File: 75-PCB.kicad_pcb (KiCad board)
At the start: 2 copper layers, 324 parts, among them J1 AVR-ISP-6, Q1 2N7002, SW1 SW_Push, U1 AT90USB1286-AU, U2 PRTR5V0U2X, Y1 16MHz

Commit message: Finished PCB edges
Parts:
- moved USB1 257.2 mm to (283.4, -240.5), turned to 180 degrees
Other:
- board outline added: 315.1 x 125.4 mm

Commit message: Changed USB connector
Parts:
- LED1, LED2, LED3, LED4, LED5, LED6, LED7, LED8, LED9, U1, U2: moved to B.Cu
- USB1: value Wurth-632723300011 -> HRO-TYPE-C-31-M-12; footprint Type-C:Wurth-632723300011-HandSoldering -> Type-C:HRO-TYPE-C-31-M-12
- moved SW1 524.7 mm to (324.6, -208.0)
- moved D1 520.4 mm to (358.8, -217.5)
- moved LED5 507.3 mm to (258.8, -231.0), turned to 270 degrees
- moved J1 498.0 mm to (283.4, -198.4)
- moved LED8 494.6 mm to (304.0, -196.1)
- moved LED4 470.0 mm to (199.2, -231.0), turned to 90 degrees
- moved LED9 454.7 mm to (304.0, -158.0)
- moved R9 454.5 mm to (392.8, -184.2)
- moved R8 445.0 mm to (384.0, -184.2)
- moved LED3 438.4 mm to (133.3, -231.0), turned to 270 degrees
- moved F1 431.8 mm to (349.1, -169.9)
- moved LED1 431.7 mm to (11.9, -231.0), turned to 90 degrees
- moved LED2 429.7 mm to (73.0, -231.0), turned to 270 degrees
- moved U2 428.9 mm to (289.7, -227.8)
- moved C11 393.7 mm to (348.3, -152.4)
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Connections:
- U1 pad 17: Net-(U1-Pad17) -> LEDMOS
- USB1 pad 10: Net-(USB1-Pad10) -> Net-(R7-Pad2)
- USB1 pad 11: Net-(USB1-Pad11) -> VCC
- USB1 pad 2: Net-(USB1-Pad2) -> VCC
- USB1 pad 4: VCC -> Net-(R6-Pad2)
- USB1 pad 5: Net-(R6-Pad2) -> Net-(R8-Pad2)
- USB1 pad 8: Net-(USB1-Pad8) -> Net-(R9-Pad2)
- USB1 pad 9: VCC -> Net-(USB1-Pad9)
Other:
- net class Default: trace_width 0.25 -> 0.254
- net class Power added: clearance 0.2, trace_width 0.381, via_dia 0.8, via_drill 0.4

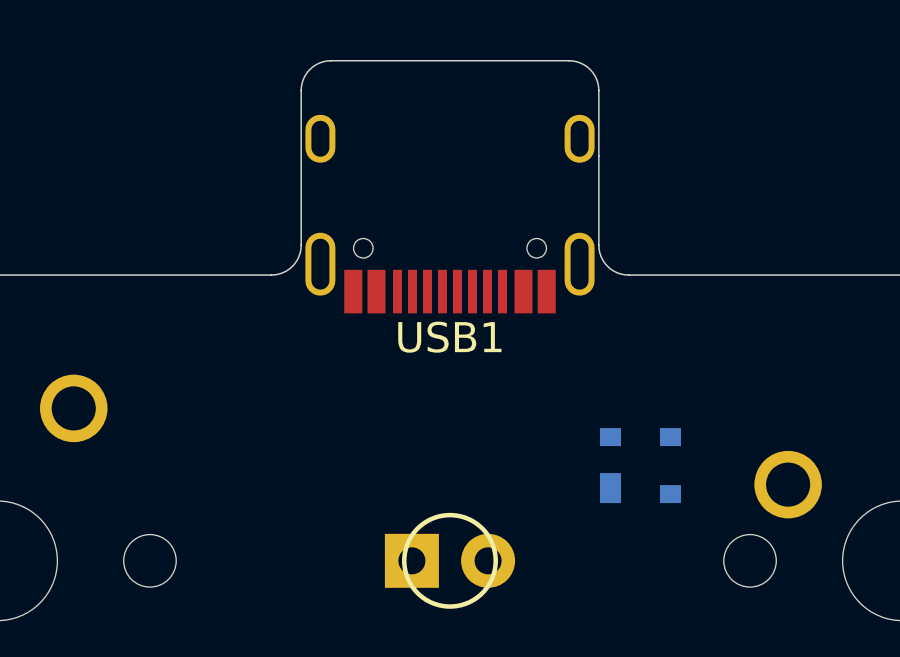
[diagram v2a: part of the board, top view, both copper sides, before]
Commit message: Changed USB connector
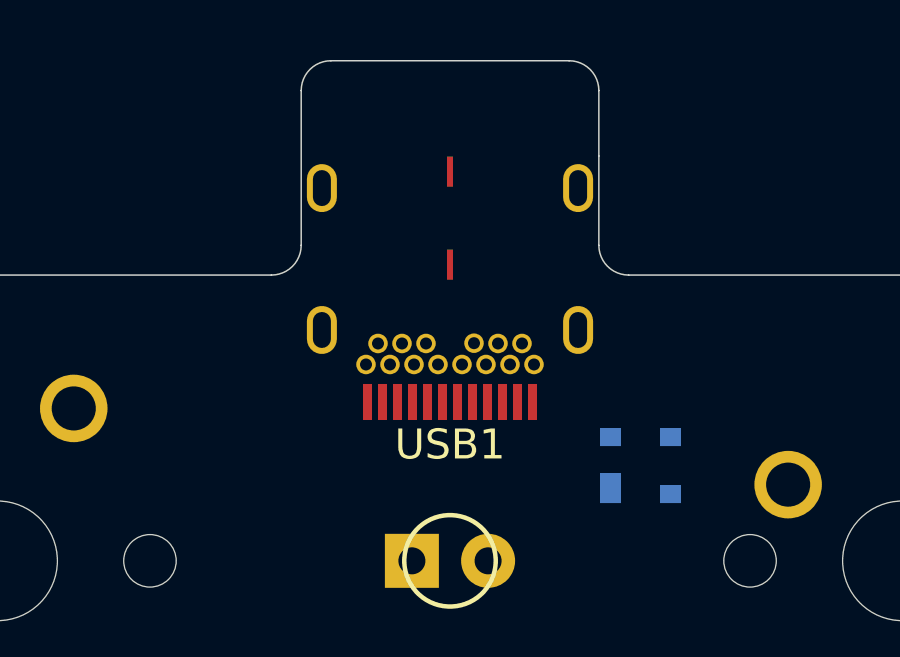
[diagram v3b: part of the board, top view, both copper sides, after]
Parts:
- USB1: value HRO-TYPE-C-31-M-12 -> Wurth-632723300011; footprint Type-C:HRO-TYPE-C-31-M-12 -> Type-C:Wurth-632723300011
- moved USB1 0.79 mm to (283.4, -240.5)
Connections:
- USB1 pad 10: Net-(R7-Pad2) -> Net-(USB1-Pad10)
- USB1 pad 11: VCC -> Net-(USB1-Pad11)
- USB1 pad 2: VCC -> Net-(USB1-Pad2)
- USB1 pad 4: Net-(R6-Pad2) -> VCC
- USB1 pad 5: Net-(R8-Pad2) -> Net-(R6-Pad2)
- USB1 pad 8: Net-(R9-Pad2) -> Net-(USB1-Pad8)
- USB1 pad 9: Net-(USB1-Pad9) -> VCC
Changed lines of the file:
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@@
     (zones 0)
     (modules 324)
-    (nets 285)
+    (nets 293)
   )
   (page A4)
@@
   (net 282 "Net-(USB1-Pad3)")
   (net 283 "Net-(MX_#0-Pad4)")
-  (net 284 "Net-(USB1-Pad9)")
+  (net 284 "Net-(USB1-Pad23)")
+  (net 285 "Net-(USB1-Pad22)")
+  (net 286 "Net-(USB1-Pad20)")
+  (net 287 "Net-(USB1-Pad15)")
+  (net 288 "Net-(USB1-Pad14)")
+  (net 289 "Net-(USB1-Pad11)")
+  (net 290 "Net-(USB1-Pad10)")
+  (net 291 "Net-(USB1-Pad8)")
+  (net 292 "Net-(USB1-Pad2)")
   (net_class Default "This is the default net class."
     (clearance 0.2)
@@
     (add_net "Net-(U1-Pad62)")
     (add_net "Net-(U1-Pad9)")
+    (add_net "Net-(USB1-Pad10)")
+    (add_net "Net-(USB1-Pad11)")
+    (add_net "Net-(USB1-Pad14)")
+    (add_net "Net-(USB1-Pad15)")
+    (add_net "Net-(USB1-Pad2)")
+    (add_net "Net-(USB1-Pad20)")
+    (add_net "Net-(USB1-Pad22)")
+    (add_net "Net-(USB1-Pad23)")
     (add_net "Net-(USB1-Pad3)")
-    (add_net "Net-(USB1-Pad9)")
+    (add_net "Net-(USB1-Pad8)")
     (add_net RESET)
     (add_net RGBLED)
@@
     (add_net VCC)
   )
-  (module Type-C:HRO-TYPE-C-31-M-12 (layer F.Cu)
-    (at 283.36875 -241.3 180)
+  (module Type-C:Wurth-632723300011 (layer F.Cu)
+    (at 283.36875 -240.50625 180)
     (attr smd)
-    (fp_text reference USB1 (at 0 -9.25) (layer F.SilkS)
+    (fp_text reference USB1 (at 0 -12) (layer F.SilkS)
       (effects (font (size 1 1) (thickness 0.15)))
     )
-    (fp_text value HRO-TYPE-C-31-M-12 (at 0 1.15) (layer Dwgs.User)
+    (fp_text value Wurth-632723300011 (at 0 1.9) (layer F.Fab)
       (effects (font (size 1 1) (thickness 0.15)))
     )
-    (fp_line (start -4.47 0) (end 4.47 0) (layer Dwgs.User) (width 0.15))
-    (fp_line (start -4.47 0) (end -4.47 -7.3) (layer Dwgs.User) (width 0.15))
-    (fp_line (start 4.47 0) (end 4.47 -7.3) (layer Dwgs.User) (width 0.15))
-    (fp_line (start -4.47 -7.3) (end 4.47 -7.3) (layer Dwgs.User) (width 0.15))
-    (pad 12 smd rect (at 3.225 -7.695 180) (size 0.6 1.45) (layers F.Cu F.Paste F.Mask)
-      (net 1 GND))
-    (pad 1 smd rect (at -3.225 -7.695 180) (size 0.6 1.45) (layers F.Cu F.Paste F.Mask)
-      (net 1 GND))
-    (pad 11 smd rect (at 2.45 -7.695 180) (size 0.6 1.45) (layers F.Cu F.Paste F.Mask)
+    (fp_line (start -4.37 0.95) (end 4.37 0.95) (layer Dwgs.User) (width 0.15))
+    (fp_line (start -4.37 0.95) (end -4.37 -10.38) (layer Dwgs.User) (width 0.15))
+    (fp_line (start 4.37 0.95) (end 4.37 -10.38) (layer Dwgs.User) (width 0.15))
+    (fp_line (start -4.37 -10.38) (end 4.37 -10.38) (layer Dwgs.User) (width 0.15))
+    (pad 27 smd rect (at 0 -2.9 180) (size 0.2 1) (layers F.Cu F.Paste F.Mask)
+      (net 1 GND))
+    (pad 27 smd rect (at 0 -6 180) (size 0.2 1) (layers F.Cu F.Paste F.Mask)
+      (net 1 GND))
+    (pad 26 thru_hole oval (at -4.27 -3.45 180) (size 1 1.6) (drill oval 0.6 1.2) (layers *.Cu B.Mask)
+      (net 1 GND))
+    (pad 26 thru_hole oval (at -4.27 -8.18 180) (size 1 1.6) (drill oval 0.6 1.2) (layers *.Cu B.Mask)
+      (net 1 GND))
+    (pad 26 thru_hole oval (at 4.27 -3.45 180) (size 1 1.6) (drill oval 0.6 1.2) (layers *.Cu B.Mask)
+      (net 1 GND))
+    (pad 26 thru_hole oval (at 4.27 -8.18 180) (size 1 1.6) (drill oval 0.6 1.2) (layers *.Cu B.Mask)
+      (net 1 GND))
+    (pad 25 thru_hole circle (at -2 -9.33 180) (size 0.65 0.65) (drill 0.4) (layers *.Cu B.Mask)
+      (net 1 GND))
+    (pad 24 thru_hole circle (at -2.8 -9.33 180) (size 0.65 0.65) (drill 0.4) (layers *.Cu B.Mask)
+      (net 1 GND))
+    (pad 23 thru_hole circle (at -2.4 -8.63 180) (size 0.65 0.65) (drill 0.4) (layers *.Cu B.Mask)
+      (net 284 "Net-(USB1-Pad23)"))
+    (pad 22 thru_hole circle (at -1.6 -8.63 180) (size 0.65 0.65) (drill 0.4) (layers *.Cu B.Mask)
+      (net 285 "Net-(USB1-Pad22)"))
+    (pad 21 thru_hole circle (at -1.2 -9.33 180) (size 0.65 0.65) (drill 0.4) (layers *.Cu B.Mask)
       (net 103 VCC))
-    (pad 2 smd rect (at -2.45 -7.695 180) (size 0.6 1.45) (layers F.Cu F.Paste F.Mask)
+    (pad 20 thru_hole circle (at -0.8 -8.62 180) (size 0.65 0.65) (drill 0.4) (layers *.Cu B.Mask)
+      (net 286 "Net-(USB1-Pad20)"))
+    (pad 19 thru_hole circle (at -0.4 -9.33 180) (size 0.65 0.65) (drill 0.4) (layers *.Cu B.Mask)
+      (net 232 "Net-(R8-Pad2)"))
+    (pad 18 thru_hole circle (at 0.4 -9.33 180) (size 0.65 0.65) (drill 0.4) (layers *.Cu B.Mask)
+      (net 234 "Net-(R9-Pad2)"))
+    (pad 17 thru_hole circle (at 0.8 -8.63 180) (size 0.65 0.65) (drill 0.4) (layers *.Cu B.Mask)
+      (net 231 "Net-(R7-Pad2)"))
+    (pad 16 thru_hole circle (at 1.2 -9.33 180) (size 0.65 0.65) (drill 0.4) (layers *.Cu B.Mask)
       (net 103 VCC))
-    (pad 3 smd rect (at -1.75 -7.695 180) (size 0.3 1.45) (layers F.Cu F.Paste F.Mask)
+    (pad 15 thru_hole circle (at 1.6 -8.63 180) (size 0.65 0.65) (drill 0.4) (layers *.Cu B.Mask)
+      (net 287 "Net-(USB1-Pad15)"))
+    (pad 25 thru_hole circle (at 2 -9.33 180) (size 0.65 0.65) (drill 0.4) (layers *.Cu B.Mask)
+      (net 1 GND))
+    (pad 14 thru_hole circle (at 2.4 -8.63 180) (size 0.65 0.65) (drill 0.4) (layers *.Cu B.Mask)
+      (net 288 "Net-(USB1-Pad14)"))
+    (pad 13 thru_hole circle (at 2.8 -9.33 180) (size 0.65 0.65) (drill 0.4) (layers *.Cu B.Mask)
+      (net 1 GND))
+    (pad 12 smd rect (at 2.75 -10.58 180) (size 0.3 1.2) (layers F.Cu F.Paste F.Mask)
+      (net 1 GND))
+    (pad 11 smd rect (at 2.25 -10.58 180) (size 0.3 1.2) (layers F.Cu F.Paste F.Mask)
+      (net 289 "Net-(USB1-Pad11)"))
+    (pad 10 smd rect (at 1.75 -10.58 180) (size 0.3 1.2) (layers F.Cu F.Paste F.Mask)
+      (net 290 "Net-(USB1-Pad10)"))
+    (pad 9 smd rect (at 1.25 -10.58 180) (size 0.3 1.2) (layers F.Cu F.Paste F.Mask)
+      (net 103 VCC))
+    (pad 8 smd rect (at 0.75 -10.58 180) (size 0.3 1.2) (layers F.Cu F.Paste F.Mask)
+      (net 291 "Net-(USB1-Pad8)"))
+    (pad 7 smd rect (at 0.25 -10.58 180) (size 0.3 1.2) (layers F.Cu F.Paste F.Mask)
+      (net 232 "Net-(R8-Pad2)"))
+    (pad 6 smd rect (at -0.25 -10.58 180) (size 0.3 1.2) (layers F.Cu F.Paste F.Mask)
+      (net 234 "Net-(R9-Pad2)"))
+    (pad 5 smd rect (at -0.75 -10.58 180) (size 0.3 1.2) (layers F.Cu F.Paste F.Mask)
+      (net 230 "Net-(R6-Pad2)"))
+    (pad 4 smd rect (at -1.25 -10.58 180) (size 0.3 1.2) (layers F.Cu F.Paste F.Mask)
+      (net 103 VCC))
+    (pad 3 smd rect (at -1.75 -10.58 180) (size 0.3 1.2) (layers F.Cu F.Paste F.Mask)
       (net 282 "Net-(USB1-Pad3)"))
-    (pad 10 smd rect (at 1.75 -7.695 180) (size 0.3 1.45) (layers F.Cu F.Paste F.Mask)
-      (net 231 "Net-(R7-Pad2)"))
-    (pad 4 smd rect (at -1.25 -7.695 180) (size 0.3 1.45) (layers F.Cu F.Paste F.Mask)
-      (net 230 "Net-(R6-Pad2)"))
-    (pad 9 smd rect (at 1.25 -7.695 180) (size 0.3 1.45) (layers F.Cu F.Paste F.Mask)
-      (net 284 "Net-(USB1-Pad9)"))
-    (pad 5 smd rect (at -0.75 -7.695 180) (size 0.3 1.45) (layers F.Cu F.Paste F.Mask)
-      (net 232 "Net-(R8-Pad2)"))
-    (pad 8 smd rect (at 0.75 -7.695 180) (size 0.3 1.45) (layers F.Cu F.Paste F.Mask)
-      (net 234 "Net-(R9-Pad2)"))
-    (pad 7 smd rect (at 0.25 -7.695 180) (size 0.3 1.45) (layers F.Cu F.Paste F.Mask)
-      (net 232 "Net-(R8-Pad2)"))
-    (pad 6 smd rect (at -0.25 -7.695 180) (size 0.3 1.45) (layers F.Cu F.Paste F.Mask)
-      (net 234 "Net-(R9-Pad2)"))
-    (pad "" np_thru_hole circle (at 2.89 -6.25 180) (size 0.65 0.65) (drill 0.65) (layers *.Cu *.Mask))
-    (pad "" np_thru_hole circle (at -2.89 -6.25 180) (size 0.65 0.65) (drill 0.65) (layers *.Cu *.Mask))
-    (pad 13 thru_hole oval (at -4.32 -6.78 180) (size 1 2.1) (drill oval 0.6 1.7) (layers *.Cu B.Mask)
-      (net 1 GND))
-    (pad 13 thru_hole oval (at 4.32 -6.78 180) (size 1 2.1) (drill oval 0.6 1.7) (layers *.Cu B.Mask)
-      (net 1 GND))
-    (pad 13 thru_hole oval (at -4.32 -2.6 180) (size 1 1.6) (drill oval 0.6 1.2) (layers *.Cu B.Mask)
-      (net 1 GND))
-    (pad 13 thru_hole oval (at 4.32 -2.6 180) (size 1 1.6) (drill oval 0.6 1.2) (layers *.Cu B.Mask)
+    (pad 2 smd rect (at -2.25 -10.58 180) (size 0.3 1.2) (layers F.Cu F.Paste F.Mask)
+      (net 292 "Net-(USB1-Pad2)"))
+    (pad 1 smd rect (at -2.75 -10.58 180) (size 0.3 1.2) (layers F.Cu F.Paste F.Mask)
       (net 1 GND))
   )

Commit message: Positioned underglow LEDs
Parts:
- moved LED5 3.18 mm to (261.9, -231.0)
- moved LED4 3.16 mm to (202.4, -231.0)
- moved LED6 1.59 mm to (-4.76, -197.6)
- moved LED8 1.59 mm to (304.0, -197.6)
- moved LED7 1.59 mm to (-4.76, -159.5)
- moved LED9 1.59 mm to (304.0, -159.5)
- moved LED1 0.79 mm to (11.1, -231.0)
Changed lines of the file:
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@@
   )
   (module WS2812B:WS2812B (layer B.Cu)
-    (at 304.00625 -157.95625)
+    (at 304.00625 -159.54375)
     (fp_text reference LED9 (at 0 4.572) (layer B.SilkS)
       (effects (font (size 1 1) (thickness 0.15)) (justify mirror))
@@
   )
   (module WS2812B:WS2812B (layer B.Cu)
-    (at 304.00625 -196.05625)
+    (at 304.00625 -197.64375)
     (fp_text reference LED8 (at 0 4.572) (layer B.SilkS)
       (effects (font (size 1 1) (thickness 0.15)) (justify mirror))
@@
   )
   (module WS2812B:WS2812B (layer B.Cu)
-    (at -4.7625 -157.95625)
+    (at -4.7625 -159.54375)
     (fp_text reference LED7 (at 0 4.572) (layer B.SilkS)
       (effects (font (size 1 1) (thickness 0.15)) (justify mirror))
@@
   )
   (module WS2812B:WS2812B (layer B.Cu)
-    (at -4.7625 -196.05625)
+    (at -4.7625 -197.64375)
     (fp_text reference LED6 (at 0 4.572) (layer B.SilkS)
       (effects (font (size 1 1) (thickness 0.15)) (justify mirror))
@@
   )
   (module WS2812B:WS2812B (layer B.Cu)
-    (at 258.7625 -230.98125 270)
+    (at 261.9375 -230.98125 270)
     (fp_text reference LED5 (at 0 4.572 270) (layer B.SilkS)
       (effects (font (size 1 1) (thickness 0.15)) (justify mirror))
@@
   )
   (module WS2812B:WS2812B (layer B.Cu)
-    (at 199.23125 -230.98125 90)
+    (at 202.3875 -231.04375 90)
     (fp_text reference LED4 (at 0 4.572 -90) (layer B.SilkS)
       (effects (font (size 1 1) (thickness 0.15)) (justify mirror))
@@
   )
   (module WS2812B:WS2812B (layer B.Cu)
-    (at 11.90625 -230.98125 90)
+    (at 11.1125 -230.98125 90)
     (fp_text reference LED1 (at 0 4.572 -90) (layer B.SilkS)
       (effects (font (size 1 1) (thickness 0.15)) (justify mirror))

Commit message: Updated switch footprints
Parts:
- MX_ENTER2: footprint MX_Only:MXOnly-ISO-ReversedStabilizers -> MX_Only:MXOnly-ISO-ROTATED-ReversedStabilizers
- MX_LALT2, MX_LCTRL2: footprint MX_Only:MXOnly-1.5U -> MX_Only:MXOnly-1.5U-FLIPPED
- MX_LWIN2: footprint MX_Only:MXOnly-1U -> MX_Only:MXOnly-1U-FLIPPED

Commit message: Finished MCU capacitor and USB traces
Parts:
- C1, C10, C11, C12, C13, C14, C15, C16, C2, C3, C4, C5, C6, C7, C8, C9, D1, F1, Q1, R10, R11, R6, R7, R8, R9, SW1, Y1: moved to B.Cu
- moved C8 443.1 mm to (16.7, -232.6)
- moved R6 440.0 mm to (288.1, -227.8), turned to 270 degrees
- moved C5 438.3 mm to (295.3, -177.0), turned to 270 degrees
- moved C9 434.4 mm to (78.6, -232.6)
- moved C12 433.9 mm to (267.5, -232.6)
- moved C15 409.1 mm to (305.6, -192.1), turned to 270 degrees
- moved C14 394.5 mm to (-6.35, -154.0), turned to 90 degrees
- moved R10 388.9 mm to (293.7, -158.0), turned to 90 degrees
- moved C13 387.0 mm to (-6.35, -192.1), turned to 270 degrees
- moved Y1 385.0 mm to (283.4, -161.1)
- moved C16 370.2 mm to (305.6, -154.0), turned to 270 degrees
- moved Q1 274.7 mm to (296.9, -158.0)
- moved R7 247.5 mm to (278.6, -227.8), turned to 270 degrees
- moved C10 208.0 mm to (138.9, -232.6)
- moved R11 176.6 mm to (293.7, -154.1), turned to 270 degrees
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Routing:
- net +5V: track 0.00 -> 79.8 mm, vias 0 -> 5
- net GND: track 0.00 -> 73.7 mm, vias 0 -> 3
- net D+: track 0.00 -> 41.0 mm
- net D-: track 0.00 -> 40.0 mm
- net VCC: track 0.00 -> 35.7 mm, vias 0 -> 1
- net Net-(R8-Pad2): track 0.00 -> 22.5 mm, vias 0 -> 1
- net Net-(R9-Pad2): track 0.00 -> 20.8 mm, vias 0 -> 2
- net Net-(C2-Pad1): track 0.00 -> 12.5 mm
- net Net-(R7-Pad2): track 0.00 -> 12.1 mm
- net Net-(C1-Pad1): track 0.00 -> 10.9 mm
- net Net-(C7-Pad1): track 0.00 -> 8.04 mm, vias 0 -> 2
- net Net-(R6-Pad2): track 0.00 -> 6.22 mm, vias 0 -> 1
- net Net-(D1-Pad2): track 0.00 -> 1.71 mm
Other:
- outline, holes or cut-outs redrawn
- net class Default: via_dia 0.8 -> 0.6
- net class Power: trace_width 0.381 -> 0.254; via_dia 0.8 -> 0.6

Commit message: Placed LED resistors
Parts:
- R13, R14, R15, R16, R17, R18, R19, R20, R21, R22, R23, R24, R25, R26, R27, R28, R29, R30, R31, R32, R33, R34, R35, R36, R37, R38, R39, R40, R41, R42, R43, R44, R45, R46, R47, R48, R49, R50, R51, R52, R53, R54, R55, R56, R57, R58, R59, R60, R61, R62, R63, R64, R65, R66, R67, R68, R69, R70, R71, R72, R73, R74, R75, R76, R77, R78, R79, R80, R81, R82, R83, R84, R85, R86, R87, R88, R89, R90, R91, R92, R93, R94, R95, R96, R97, R98, R99: moved to B.Cu
- moved R94 450.1 mm to (303.2, -220.7), turned to 90 degrees
- moved R13 436.5 mm to (6.35, -220.7), turned to 90 degrees
- moved R25 434.2 mm to (49.2, -220.7), turned to 90 degrees
- moved R71 432.5 mm to (211.1, -220.7), turned to 90 degrees
- moved R95 427.8 mm to (293.7, -201.6), turned to 90 degrees
- moved R48 422.8 mm to (130.2, -220.7), turned to 90 degrees
- moved R96 421.9 mm to (303.2, -182.6), turned to 90 degrees
- moved R42 421.7 mm to (111.1, -220.7), turned to 90 degrees
- moved R54 421.6 mm to (149.2, -220.7), turned to 90 degrees
- moved R77 420.8 mm to (230.2, -220.7), turned to 90 degrees
- moved R14 420.8 mm to (6.35, -201.6), turned to 90 degrees
- moved R65 416.2 mm to (192.1, -220.7), turned to 90 degrees
- moved R83 412.0 mm to (234.9, -201.6), turned to 90 degrees
- moved R72 411.9 mm to (196.8, -201.6), turned to 90 degrees
- moved R37 411.8 mm to (82.5, -201.6), turned to 90 degrees
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
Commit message: Finished switch and LED matrix traces
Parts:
- D10, D11, D12, D13, D14, D15, D16, D17, D18, D19, D2, D20, D21, D22, D23, D24, D25, D26, D27, D28, D29, D3, D30, D31, D32, D33, D34, D35, D36, D37, D38, D39, D4, D40, D41, D42, D43, D44, D45, D46, D47, D48, D49, D5, D50, D51, D52, D53, D54, D55, D56, D57, D58, D59, D6, D60, D61, D62, D63, D64, D65, D66, D67, D68, D69, D7, D70, D71, D72, D73, D74, D75, D76, D77, D78, D79, D8, D80, D81, D82, D83, D84, D85, D89, D9, D90, D91, R1, R12, R2, R3, R4, R5: moved to B.Cu
- moved D83 481.9 mm to (297.7, -231.8)
- moved D76 460.6 mm to (276.2, -223.8), turned to 90 degrees
- moved D80 455.8 mm to (276.2, -204.8), turned to 90 degrees
- moved D71 454.1 mm to (252.4, -223.8), turned to 90 degrees
- moved D60 449.5 mm to (214.3, -223.8), turned to 90 degrees
- moved D54 447.2 mm to (195.3, -223.8), turned to 90 degrees
- moved D43 441.9 mm to (152.4, -223.8), turned to 90 degrees
- moved D66 438.1 mm to (233.4, -223.8), turned to 90 degrees
- moved D77 435.4 mm to (241.3, -204.8), turned to 90 degrees
- moved D72 429.0 mm to (238.1, -204.8), turned to 90 degrees
- moved D31 427.8 mm to (114.3, -223.8), turned to 90 degrees
- moved D8 427.6 mm to (33.3, -223.8), turned to 90 degrees
- moved D48 426.9 mm to (171.4, -223.8), turned to 90 degrees
- moved D14 426.7 mm to (52.4, -223.8), turned to 90 degrees
- moved D2 423.6 mm to (9.53, -223.8), turned to 90 degrees
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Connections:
- MX_ENTER1 pad 1: COL12 -> COL14
- MX_ENTER2 pad 1: COL12 -> COL14
- MX_LEFT1 pad 1: COL13 -> COL12
- MX_RALT1 pad 1: COL8 -> COL9
- MX_RALT2 pad 1: COL10 -> COL9
- MX_RALT2 pad 2: Net-(D65-Pad2) -> Net-(D53-Pad2)
- MX_RALT2 pad 4: Net-(MX_RALT2-Pad4) -> Net-(MX_RALT1-Pad4)
- MX_RCTRL1 pad 1: COL10 -> COL11
- MX_RCTRL1 pad 4: Net-(MX_RALT2-Pad4) -> Net-(MX_RCTRL1-Pad4)
- MX_RCTRL2 pad 1: COL8 -> COL11
- MX_RCTRL2 pad 2: Net-(D53-Pad2) -> Net-(D65-Pad2)
- MX_RCTRL2 pad 4: Net-(MX_RALT1-Pad4) -> Net-(MX_RCTRL1-Pad4)
- MX_RWIN1 pad 1: COL9 -> COL10
- MX_SPACE1 pad 1: COL5 -> COL6
- MX_SPACE2 pad 1: COL5 -> COL6
- MX_SPACE3 pad 1: COL5 -> COL6
- MX_SPACE4 pad 1: COL5 -> COL6
- MX_SPACE6 pad 1: Net-(MX_SPACE6-Pad1) -> COL8
- R76 pad 1: Net-(MX_RALT2-Pad4) -> Net-(MX_RCTRL1-Pad4)
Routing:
- net LEDGND: track 0.00 -> 1695.9 mm
- net ROW4: track 0.00 -> 299.5 mm
- net ROW5: track 0.00 -> 288.8 mm
- net ROW1: track 0.00 -> 266.7 mm
- net ROW0: track 0.00 -> 266.7 mm
- net ROW2: track 0.00 -> 236.5 mm
- net ROW3: track 0.00 -> 215.9 mm
- net COL6: track 0.00 -> 131.1 mm
- net COL11: track 0.00 -> 119.7 mm
- net COL10: track 0.00 -> 118.2 mm
- net COL9: track 0.00 -> 118.2 mm
- net COL2: track 0.00 -> 112.5 mm
- net COL14: track 0.00 -> 111.2 mm
- net COL1: track 0.00 -> 110.5 mm
- net COL4: track 0.00 -> 110.2 mm
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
